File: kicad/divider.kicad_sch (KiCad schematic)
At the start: 28 parts, among them J40 SPI, Q17 2N3904, Q18 2N3904, Q2 2N3904, Q3 2N3904, Q4 2N3904, Q5 2N3904, Q6 2N3904, Q7 2N3904, Q8 2N3904, U12 ATtiny24A-P

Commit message: Finished most recent redesign
probably still needs fixing though
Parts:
- removed R69, R71, R73, R75, R77, R79, R81: 1k8, rumblesan-standard-parts:R_Axial_DIN0207_L6.3mm_D2.5mm_P10.16mm_Horizontal, symbol rumblesan-standard-parts:R
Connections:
- net DIV13: now also Q17.1 (E)
- net DIV2: now also Q4.1 (E)
- net DIV3: now also Q6.1 (E)
- net DIV4: now also Q8.1 (E)
- net DIV5: now also Q18.1 (E)
- net DIV7: now also Q5.1 (E)
- net DIV8: now also Q7.1 (E)
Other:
- moved on the sheet: Q17, Q5, Q7, R70, R72, R74, R76, R78, R80, R82

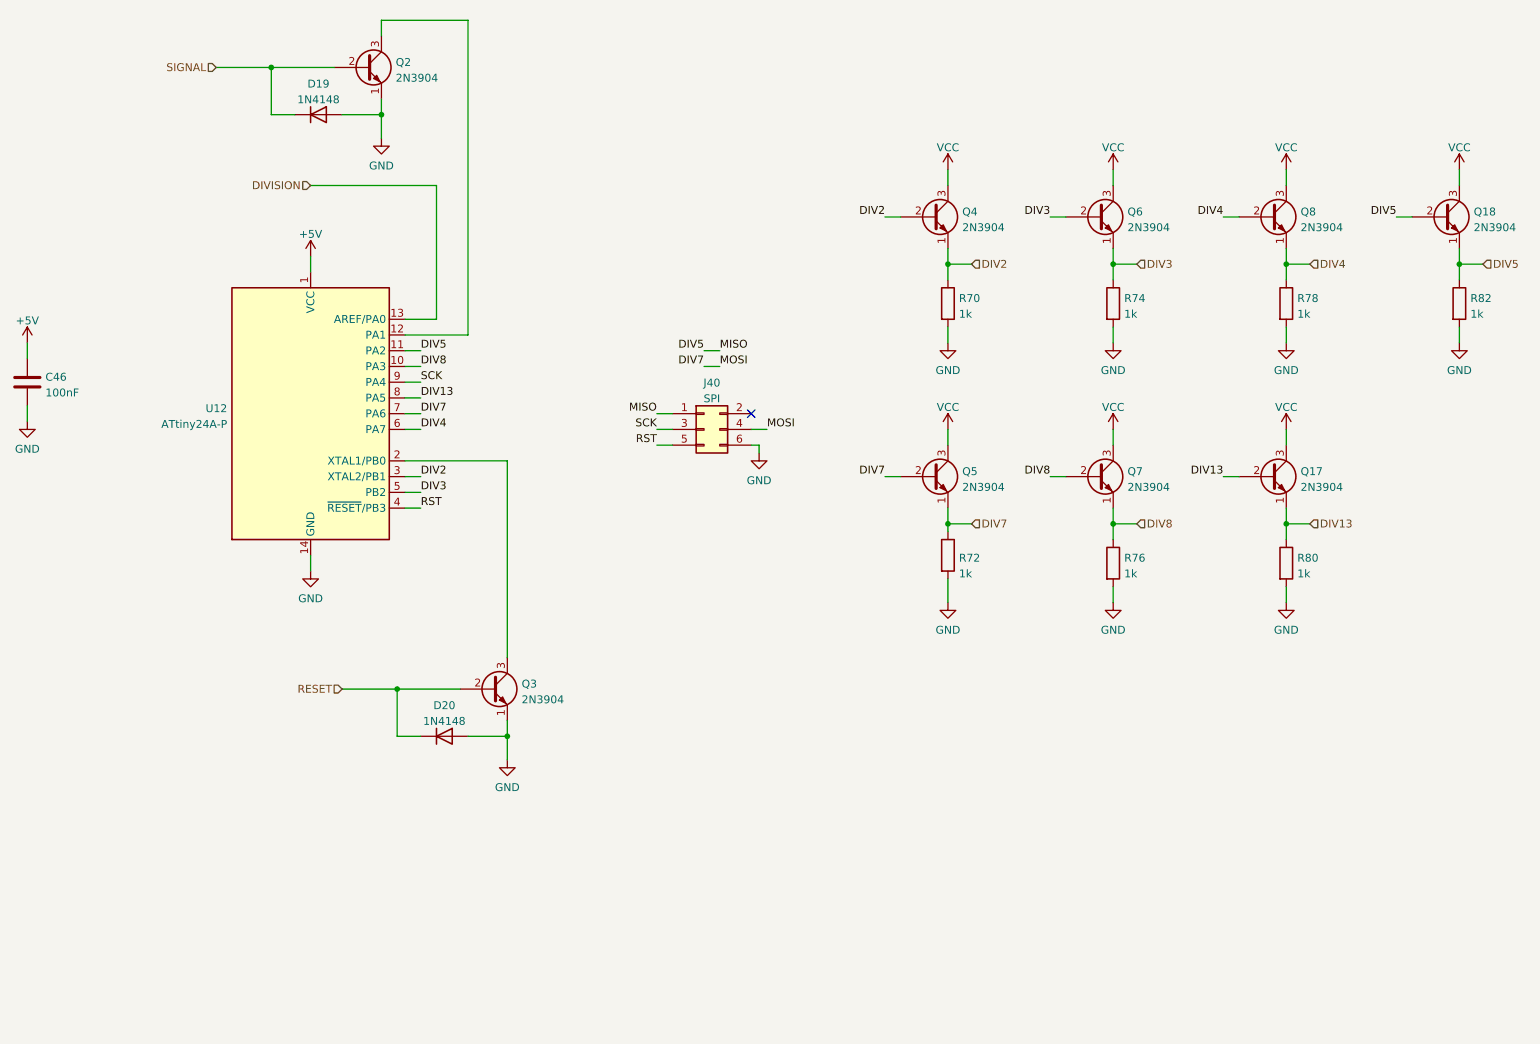
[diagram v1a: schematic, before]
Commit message: Layout seems to be all done, though needs further checking
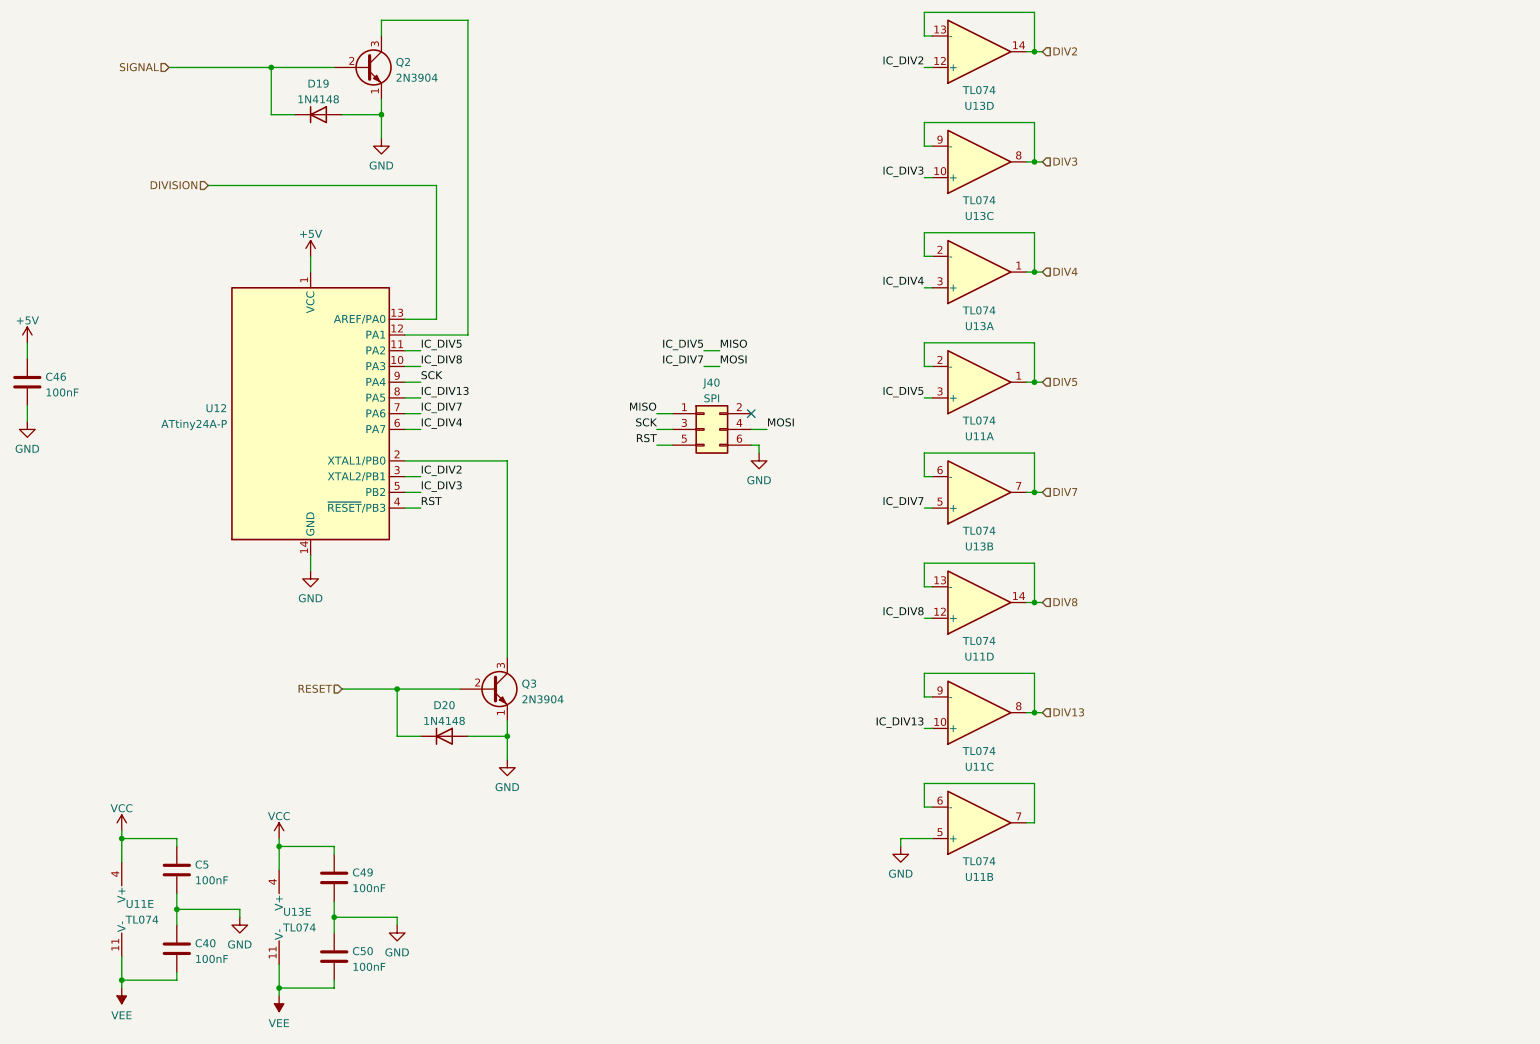
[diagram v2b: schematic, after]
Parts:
- removed Q17, Q18, Q4, Q5, Q6, Q7, Q8: 2N3904, rumblesan-standard-parts:TO-92_Inline_Wide, symbol Transistor_BJT:2N3904
- removed R70, R72, R74, R76, R78, R80, R82: 1k, rumblesan-standard-parts:R_Axial_DIN0207_L6.3mm_D2.5mm_P10.16mm_Horizontal, symbol rumblesan-standard-parts:R
- added C40, C49, C5, C50: 100nF, rumblesan-standard-parts:C_Rect_L7.0mm_W2.5mm_P5.00mm, symbol rumblesan-standard-parts:C
- added U11, U13: TL074, rumblesan-standard-parts:DIP-14_W7.62mm_Socket, symbol Amplifier_Operational:TL074
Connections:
- net DIV13: now also U11.8, U11.9 (-); no longer U12.8 (PA5)
- net DIV2: now also U13.13 (-), U13.14; no longer U12.3 (XTAL2/PB1)
- net DIV3: now also U13.8, U13.9 (-); no longer U12.5 (PB2)
- net DIV4: now also U13.1, U13.2 (-); no longer U12.6 (PA7)
- net DIV5: now also U11.1, U11.2 (-); no longer J40.1 (Pin_1), U12.11 (PA2)
- net DIV7: now also U13.6 (-), U13.7; no longer J40.4 (Pin_4), U12.7 (PA6)
- net DIV8: now also U11.13 (-), U11.14; no longer U12.10 (PA3)
- net GND: now also C40.1, C49.2, C5.2, C50.1, U11.5 (+)
- net VCC: now also C49.1, C5.1, U11.4 (V+), U13.4 (V+)
- new net: U11.6 (-), U11.7
- new net IC_DIV13: U11.10 (+), U12.8 (PA5)
- new net IC_DIV2: U12.3 (XTAL2/PB1), U13.12 (+)
- new net IC_DIV3: U12.5 (PB2), U13.10 (+)
- new net IC_DIV4: U12.6 (PA7), U13.3 (+)
- new net IC_DIV5: J40.1 (Pin_1), U11.3 (+), U12.11 (PA2)
- new net IC_DIV7: J40.4 (Pin_4), U12.7 (PA6), U13.5 (+)
- new net IC_DIV8: U11.12 (+), U12.10 (PA3)
- new net VEE: C40.2, C50.2, U11.11 (V-), U13.11 (V-)

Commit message: Updating layout again
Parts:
- removed C40, C49, C50: 100nF, rumblesan-standard-parts:C_Rect_L7.0mm_W2.5mm_P5.00mm, symbol rumblesan-standard-parts:C
- removed U11, U13: TL074, rumblesan-standard-parts:DIP-14_W7.62mm_Socket, symbol Amplifier_Operational:TL074
- added JP1: Jumper_2_Bridged, Connector_PinHeader_2.54mm:PinHeader_1x02_P2.54mm_Vertical, symbol Jumper:Jumper_2_Bridged
- added U11: 74LS241, Package_DIP:DIP-20_W7.62mm_Socket, symbol 74xx:74LS241
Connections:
- net VCC is gone; now on net +5V: C5.1
- net +5V: now also JP1.2 (B), U11.20 (VCC), U11.4 (I1a)
- net DIV13: now also U11.12 (O3a)
- net DIV2: now also U11.18 (O0a)
- net DIV3: now also U11.3 (O3b)
- net DIV4: now also U11.5 (O2b)
- net DIV5: now also U11.9 (O0b)
- net DIV7: now also U11.7 (O1b)
- net DIV8: now also U11.14 (O2a)
- net GND: now also U11.1 (OEa), U11.10 (GND), U11.19 (OEb)
- net IC_DIV13: now also U11.8 (I3a)
- net IC_DIV2: now also U11.2 (I0a)
- net IC_DIV3: now also U11.17 (I3b)
- net IC_DIV4: now also U11.15 (I2b)
- net IC_DIV5: now also U11.11 (I0b)
- net IC_DIV7: now also U11.13 (I1b)
- net IC_DIV8: now also U11.6 (I2a)
- net at J40.2 (Pin_2): now also JP1.1 (A)

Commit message: Changing name to the mercurial machine
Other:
- title: (none) -> The Mercurial Machine
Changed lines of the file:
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@@
 (kicad_sch (version 20211123) (generator eeschema)
   (paper "A4")
+  (title_block
+    (title "The Mercurial Machine")
+    (date "2023-05-13")
+    (rev "r02")
+    (comment 2 "creativecommons.org/licenses/by/4.0/")
+    (comment 3 "License: CC BY 4.0")
+    (comment 4 "Author: Guy John")
+  )
   (junction (at 86.36 128.27) (diameter 0) (color 0 0 0 0)
   )

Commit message: geographically reannotate parts
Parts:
- renumbered C46 to C47, C5 to C53, D19 to D14, D20 to D17, J40 to J39, Q2 to Q6, Q3 to Q8, U12 to U11, U11 to U14
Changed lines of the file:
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@@
   (symbol (lib_id "Connector_Generic:Conn_02x03_Odd_Even") (at 135.89 86.36 0) (unit 1)
     (in_bom yes) (on_board yes) (fields_autoplaced)
-    (property "Reference" "J40" (id 0) (at 137.16 78.8502 0))
+    (property "Reference" "J39" (id 0) (at 137.16 78.8502 0))
     (property "Value" "SPI" (id 1) (at 137.16 81.3871 0))
     (property "Footprint" "Connector_PinHeader_2.54mm:PinHeader_2x03_P2.54mm_Vertical" (id 2) (at 135.89 86.36 0)
@@
   (symbol (lib_id "rumblesan-standard-parts:C") (at 26.67 78.74 0) (unit 1)
     (in_bom yes) (on_board yes) (fields_autoplaced)
-    (property "Reference" "C46" (id 0) (at 29.591 77.9053 0)
+    (property "Reference" "C47" (id 0) (at 29.591 77.9053 0)
       (effects (font (size 1.27 1.27)) (justify left))
     )
@@
   (symbol (lib_id "74xx:74LS241") (at 234.95 90.17 0) (unit 1)
     (in_bom yes) (on_board yes) (fields_autoplaced)
-    (property "Reference" "U11" (id 0) (at 236.9694 71.2302 0)
+    (property "Reference" "U14" (id 0) (at 236.9694 71.2302 0)
       (effects (font (size 1.27 1.27)) (justify left))
     )
@@
   (symbol (lib_id "Device:D") (at 93.98 135.89 0) (unit 1)
     (in_bom yes) (on_board yes) (fields_autoplaced)
-    (property "Reference" "D20" (id 0) (at 93.98 130.9202 0))
+    (property "Reference" "D17" (id 0) (at 93.98 130.9202 0))
     (property "Value" "1N4148" (id 1) (at 93.98 133.4571 0))
     (property "Footprint" "rumblesan-standard-parts:D_DO-35_SOD27_P7.62mm_Horizontal" (id 2) (at 93.98 135.89 0)
@@
   (symbol (lib_id "Transistor_BJT:2N3904") (at 101.6 128.27 0) (unit 1)
     (in_bom yes) (on_board yes) (fields_autoplaced)
-    (property "Reference" "Q3" (id 0) (at 106.4514 127.4353 0)
+    (property "Reference" "Q8" (id 0) (at 106.4514 127.4353 0)
       (effects (font (size 1.27 1.27)) (justify left))
     )
@@
   (symbol (lib_id "Device:D") (at 73.66 35.56 0) (unit 1)
     (in_bom yes) (on_board yes) (fields_autoplaced)
-    (property "Reference" "D19" (id 0) (at 73.66 30.5902 0))
+    (property "Reference" "D14" (id 0) (at 73.66 30.5902 0))
     (property "Value" "1N4148" (id 1) (at 73.66 33.1271 0))
     (property "Footprint" "rumblesan-standard-parts:D_DO-35_SOD27_P7.62mm_Horizontal" (id 2) (at 73.66 35.56 0)
@@
   (symbol (lib_id "Transistor_BJT:2N3904") (at 81.28 27.94 0) (unit 1)
     (in_bom yes) (on_board yes) (fields_autoplaced)
-    (property "Reference" "Q2" (id 0) (at 86.1314 27.1053 0)
+    (property "Reference" "Q6" (id 0) (at 86.1314 27.1053 0)
       (effects (font (size 1.27 1.27)) (justify left))
     )
@@
   (symbol (lib_id "MCU_Microchip_ATtiny:ATtiny24A-P") (at 72.39 83.82 0) (unit 1)
     (in_bom yes) (on_board yes) (fields_autoplaced)
-    (property "Reference" "U12" (id 0) (at 58.9281 82.9853 0)
+    (property "Reference" "U11" (id 0) (at 58.9281 82.9853 0)
       (effects (font (size 1.27 1.27)) (justify right))
     )
@@
   (symbol (lib_id "rumblesan-standard-parts:C") (at 255.27 53.34 0) (unit 1)
     (in_bom yes) (on_board yes) (fields_autoplaced)
-    (property "Reference" "C5" (id 0) (at 258.191 52.5053 0)
-      (effects (font (size 1.27 1.27)) (justify left))
-    )
+    (property "Reference" "C53" (id 0) (at 258.191 52.5053 0)
+      (effects (font (size 1.27 1.27)) (justify left))
+    )

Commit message: Changing name again
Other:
- title: The Mercurial Machine -> Ouroboros
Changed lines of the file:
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@@
   (paper "A4")
   (title_block
-    (title "The Mercurial Machine")
+    (title "Ouroboros")
     (date "2023-05-13")
     (rev "r02")

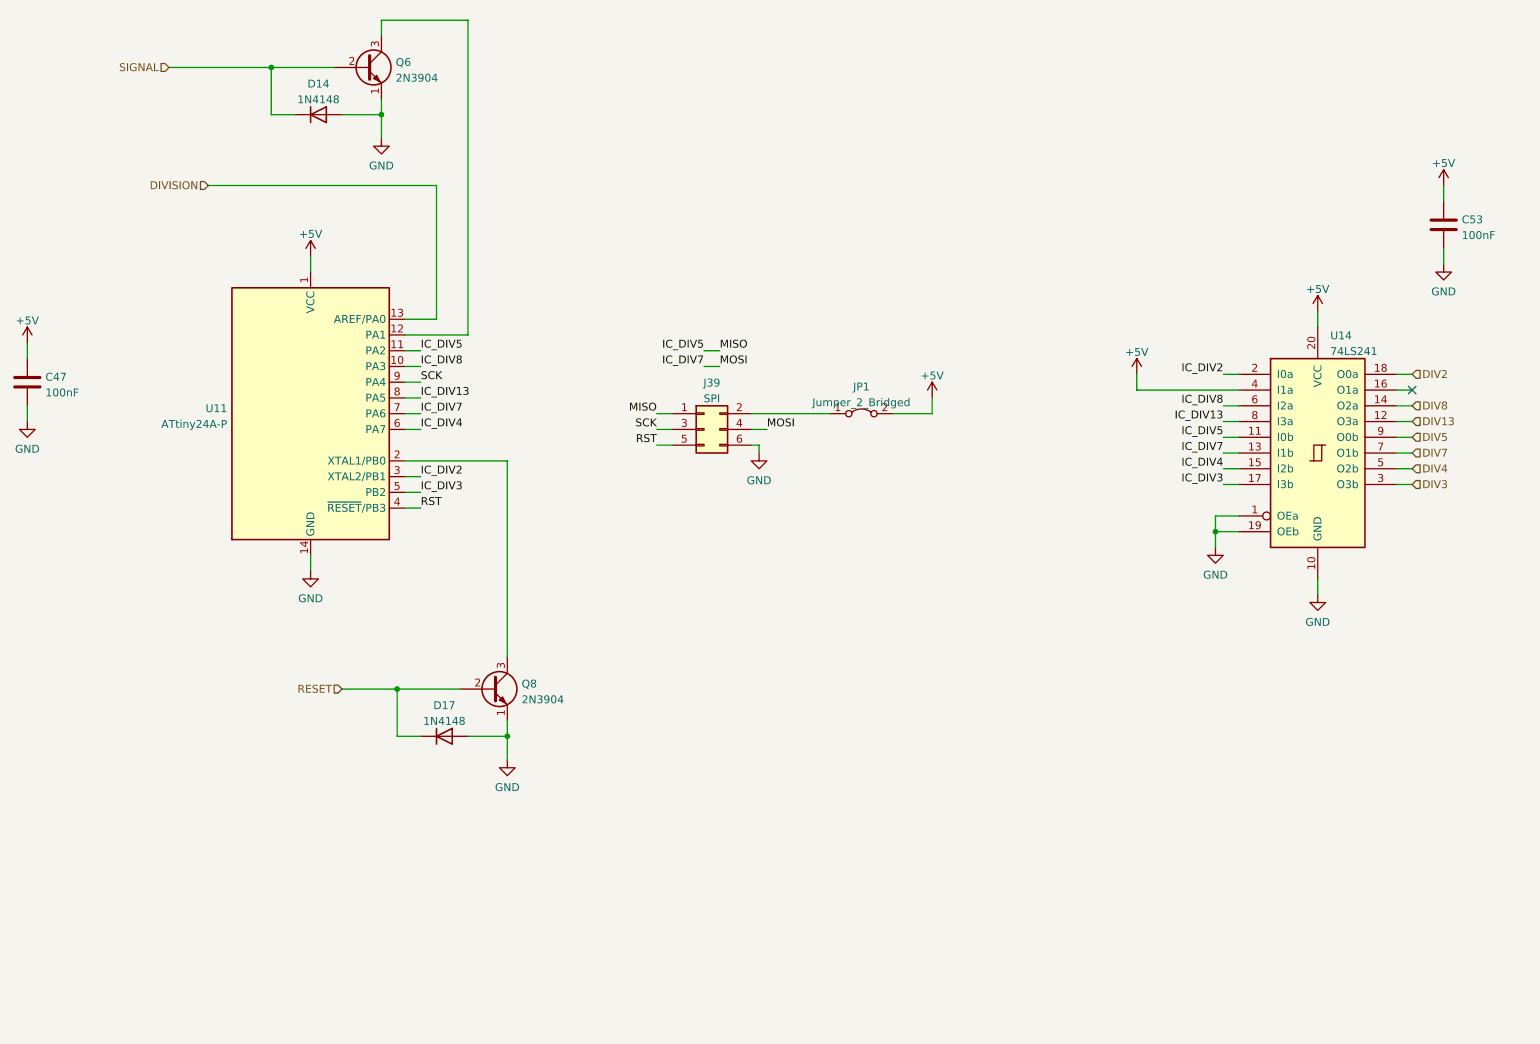
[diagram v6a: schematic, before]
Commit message: Updating for kicad 7
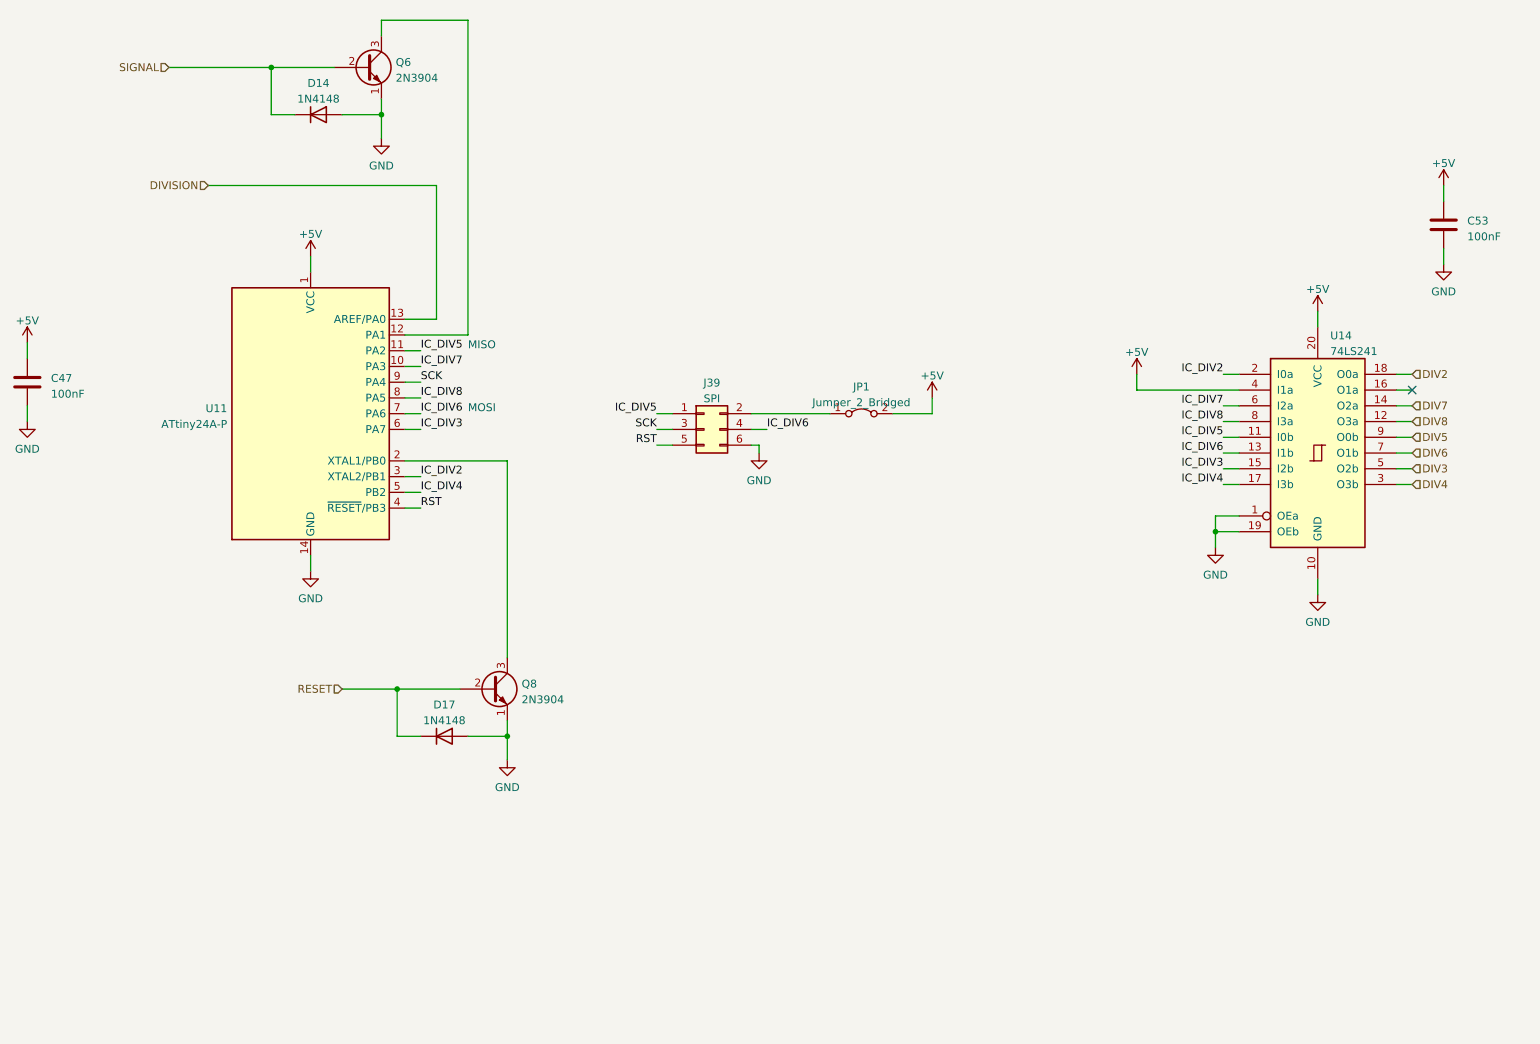
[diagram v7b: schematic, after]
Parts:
- C47, C53: footprint rumblesan-standard-parts:C_Rect_L7.0mm_W2.5mm_P5.00mm -> Rumblesan_Standard_Parts:C_Rect_L7.0mm_W2.5mm_P5.00mm; symbol rumblesan-standard-parts:C -> Rumblesan Standard Parts:C; Spec ceramic X7R -> ceramic C0G
- D14, D17: footprint rumblesan-standard-parts:D_DO-35_SOD27_P7.62mm_Horizontal -> Rumblesan_Standard_Parts:D_DO-35_SOD27_P7.62mm_Horizontal
- Q6, Q8: footprint rumblesan-standard-parts:TO-92_Inline_Wide -> Rumblesan_Standard_Parts:TO-92_Inline_Wide
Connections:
- net DIV13 is gone; now on net DIV8: U14.12 (O3a)
- net IC_DIV13 is gone; now on net IC_DIV8: U11.8 (PA5), U14.8 (I3a)
- net DIV3: now also U14.5 (O2b); no longer U14.3 (O3b)
- net DIV4: now also U14.3 (O3b); no longer U14.5 (O2b)
- net DIV7: now also U14.14 (O2a); no longer U14.7 (O1b)
- net DIV8: no longer U14.14 (O2a)
- net IC_DIV3: now also U11.6 (PA7), U14.15 (I2b); no longer U11.5 (PB2), U14.17 (I3b)
- net IC_DIV4: now also U11.5 (PB2), U14.17 (I3b); no longer U11.6 (PA7), U14.15 (I2b)
- net IC_DIV7: now also U11.10 (PA3), U14.6 (I2a); no longer J39.4 (Pin_4), U11.7 (PA6), U14.13 (I1b)
- net IC_DIV8: no longer U11.10 (PA3), U14.6 (I2a)
- new net DIV6: U14.7 (O1b)
- new net IC_DIV6: J39.4 (Pin_4), U11.7 (PA6), U14.13 (I1b)
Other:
- note added: "MISO"
- note added: "MOSI"
